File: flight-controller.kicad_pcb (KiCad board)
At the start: 4 copper layers, 60 x 60 mm, 95 parts, among them IC2 MCP2562FD-E_SN, J1 Conn_01x05, J2 USB4105-GF-A-120, J3 Conn_01x03, J4 Conn_01x04, J5 5055780271, SW1 RESET BUTTON, SW2 BOOT BUTTON, U1 STM32G474RETx, U2 TLV75533PDBVR, U3 W25Q128JVSIQ, U5 TPS259470ARPWR, U6 BMI323, U7 INA180A3IDBVR, U8 TPS2113ADRBT, Y1 ECS-80-12-33-JGN-TR3

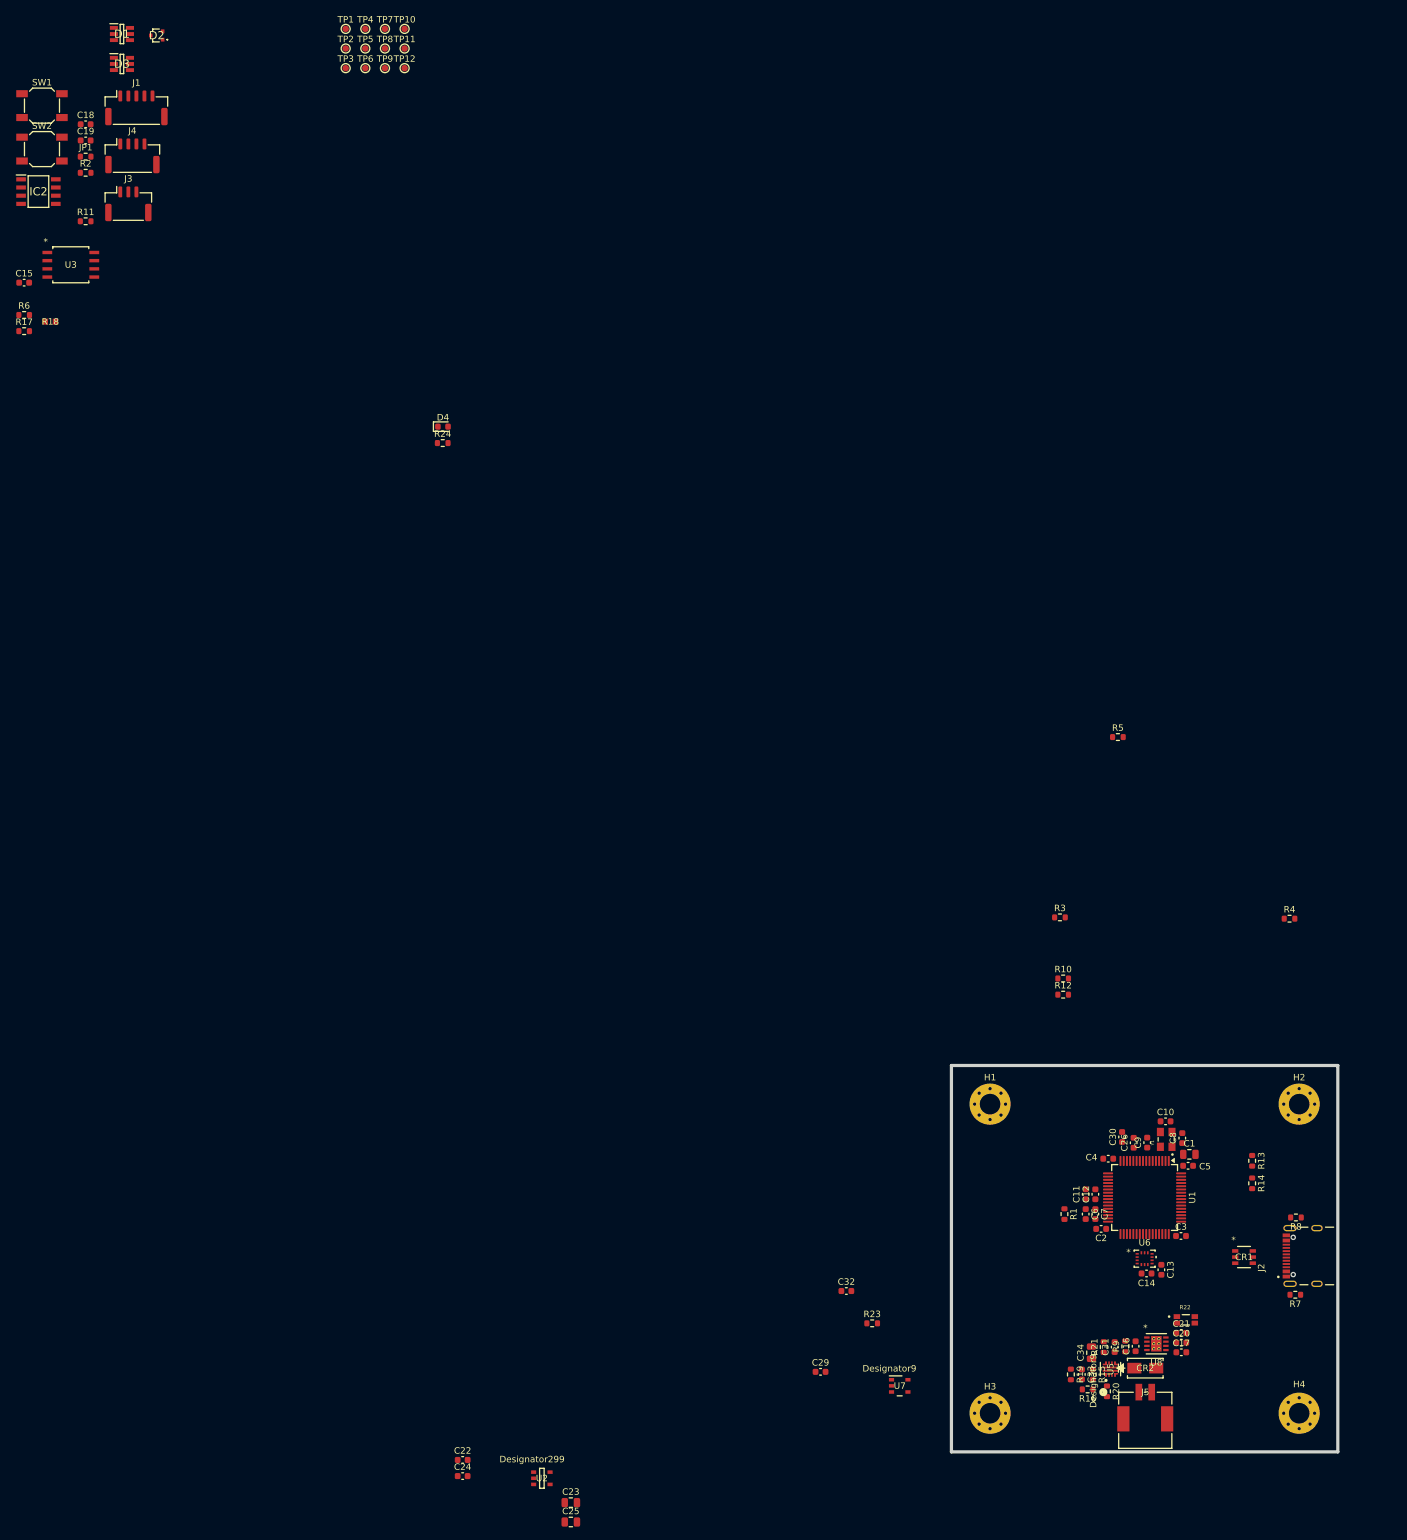
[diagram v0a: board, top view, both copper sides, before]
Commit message: Finished PCB Component Placement
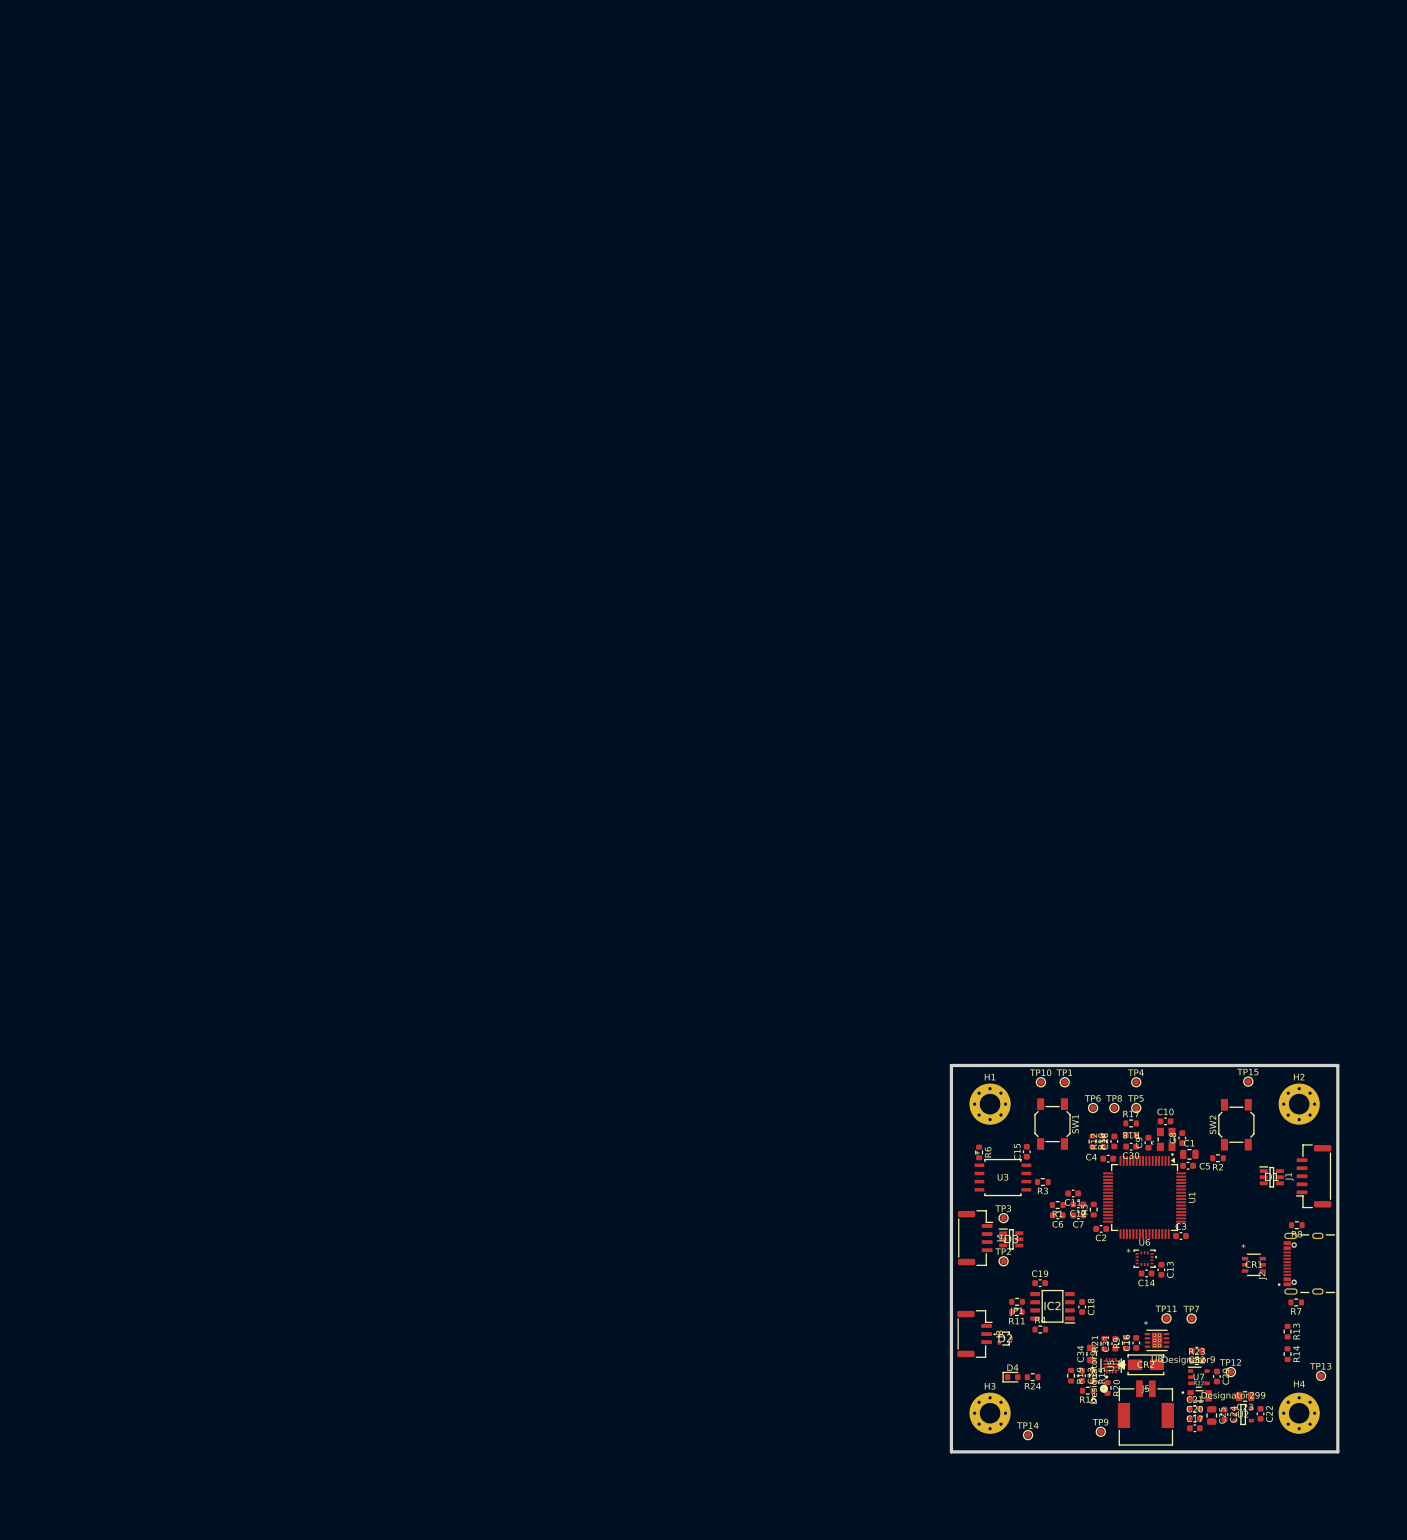
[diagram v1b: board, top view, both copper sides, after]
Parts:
- added TP13: TestPoint, TestPoint:TestPoint_Pad_D1.0mm, F.Cu at (177.4, 118.2)
- added TP14: TestPoint, TestPoint:TestPoint_Pad_D1.0mm, F.Cu at (131.9, 127.4)
- added TP15: TestPoint, TestPoint:TestPoint_Pad_D1.0mm, F.Cu at (166.1, 72.5)
- moved D1 251.8 mm to (169.8, 87.3)
- moved J1 246.9 mm to (176.3, 87.2), turned to 90 degrees
- moved D2 241.5 mm to (128.3, 112.4), turned to 180 degrees
- moved C18 240.2 mm to (140.3, 107.5), turned to -90 degrees
- moved TP12 239.7 mm to (163.4, 117.6)
- moved SW2 239.5 mm to (164.2, 79.2), turned to 90 degrees
- moved TP9 239.2 mm to (143.2, 126.9)
- moved TP7 236.2 mm to (157.3, 109.3)
- moved IC2 234.0 mm to (135.7, 107.4), turned to 180 degrees
- moved R2 233.1 mm to (161.4, 84.4), turned to 180 degrees
- moved C19 231.2 mm to (133.8, 103.8)
- moved TP11 230.0 mm to (153.4, 109.3)
- moved JP1 229.2 mm to (130.2, 106.7), turned to 180 degrees
- moved D3 228.9 mm to (129.3, 97.0)
- moved SW1 222.8 mm to (135.7, 79.1), turned to -90 degrees
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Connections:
- net CAN_H renamed CAN+
- net CAN_L renamed CAN-
- D1 pad 1: SWCLK -> NRST
- D1 pad 3: SWDIO -> SWCLK
- D1 pad 6: NRST -> SWDIO
- D3 pad 1: UART3_TX -> UART3_RX
- D3 pad 3: UART3_RX -> UART3_TX
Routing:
- added copper zone on In1.Cu, net GND

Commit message: COMPLETED THE PCB WOOOO
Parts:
- moved R13 2.67 mm to (172.2, 114.0)
- moved R14 2.47 mm to (172.2, 117.3)
- moved CR1 2.44 mm to (164.6, 100.2), turned to 180 degrees
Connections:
- CR1 pad 1: D+ -> D-
- CR1 pad 3: D- -> D+
- CR1 pad 4: D- -> D+
- CR1 pad 6: D+ -> D-
- U8 pad 1: GND -> unconnected-(U8-STAT-Pad1)
- U8 pad 3: GND -> EXT_5V
- U8 pad 4: GND -> Net-(U8-ILIM)
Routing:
- net +5V_LOAD: track 0.00 -> 97.8 mm, vias 0 -> 4
- net +3V3: track 0.00 -> 86.1 mm, vias 0 -> 15
- net USB_5V: track 0.00 -> 80.0 mm, vias 0 -> 3
- net NRST: track 0.00 -> 74.6 mm, vias 0 -> 2
- net I_SENSE_ADC: track 0.00 -> 55.4 mm, vias 0 -> 3
- net GND: track 0.00 -> 41.8 mm, vias 0 -> 23
- net CAN_STBY: track 0.00 -> 37.0 mm, vias 0 -> 2
- net Net-(U1-PC6): track 0.00 -> 34.5 mm, vias 0 -> 2
- net FDCAN2_TX: track 0.00 -> 34.5 mm, vias 0 -> 2
- net SWDIO: track 0.00 -> 31.5 mm
- net Net-(U1-PA9): track 0.00 -> 31.4 mm, vias 0 -> 2
- net FDCAN2_RX: track 0.00 -> 30.9 mm, vias 0 -> 2
- net QSPI_NCS: track 0.00 -> 27.8 mm, vias 0 -> 2
- net EXT_5V_RAW: track 0.00 -> 26.8 mm
- net D-: track 0.00 -> 25.9 mm
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- added copper zone on In2.Cu, net +3V3
- added copper zone on B.Cu, net GND
- added copper zone on F.Cu, net GND
